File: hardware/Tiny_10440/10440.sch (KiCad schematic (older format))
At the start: 48 parts, among them J2 Battery, J3 GPIO, J4 USB_B_Micro, J5 LEDs, J7 GPIO/Power, Q1 BSS806N, Q2 BSS806N, Q3 BSS806N, Q4 BSS806N, SW1 Mode, SW2 Power, U1 STM32L072KZUx, U2 AP2210N-3.3TRG1, U3 MCP73831T-2ACI_OT, U4 ESD7002WTT1G

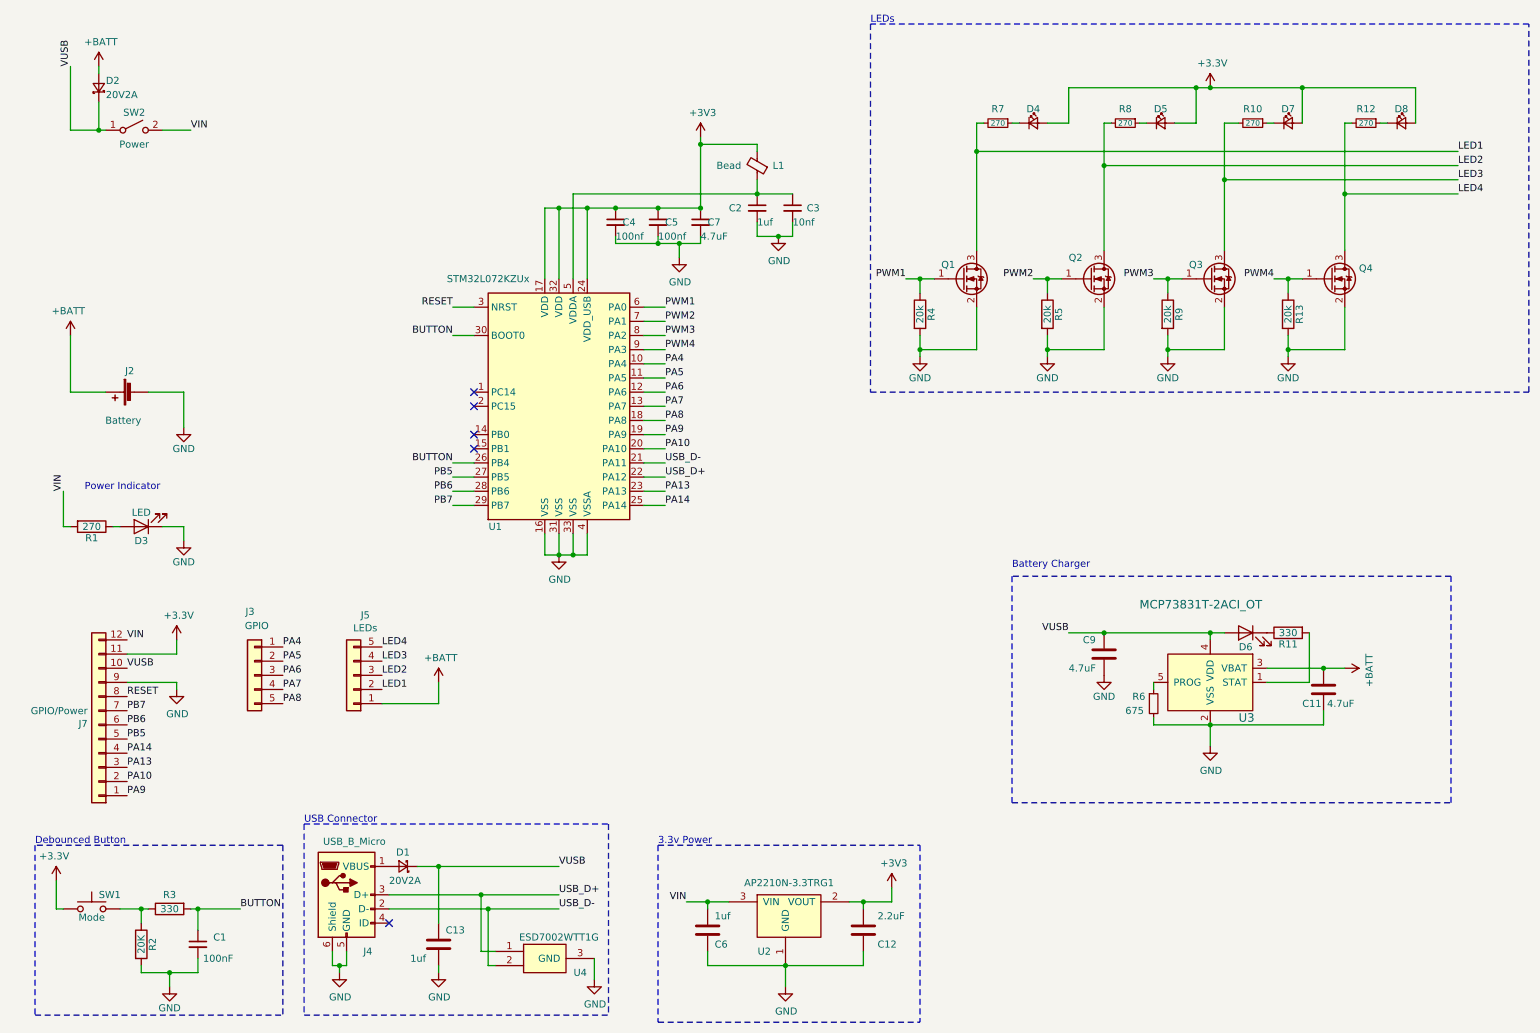
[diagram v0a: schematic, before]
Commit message: Use STM32F412CGUx (Regular & Tiny)
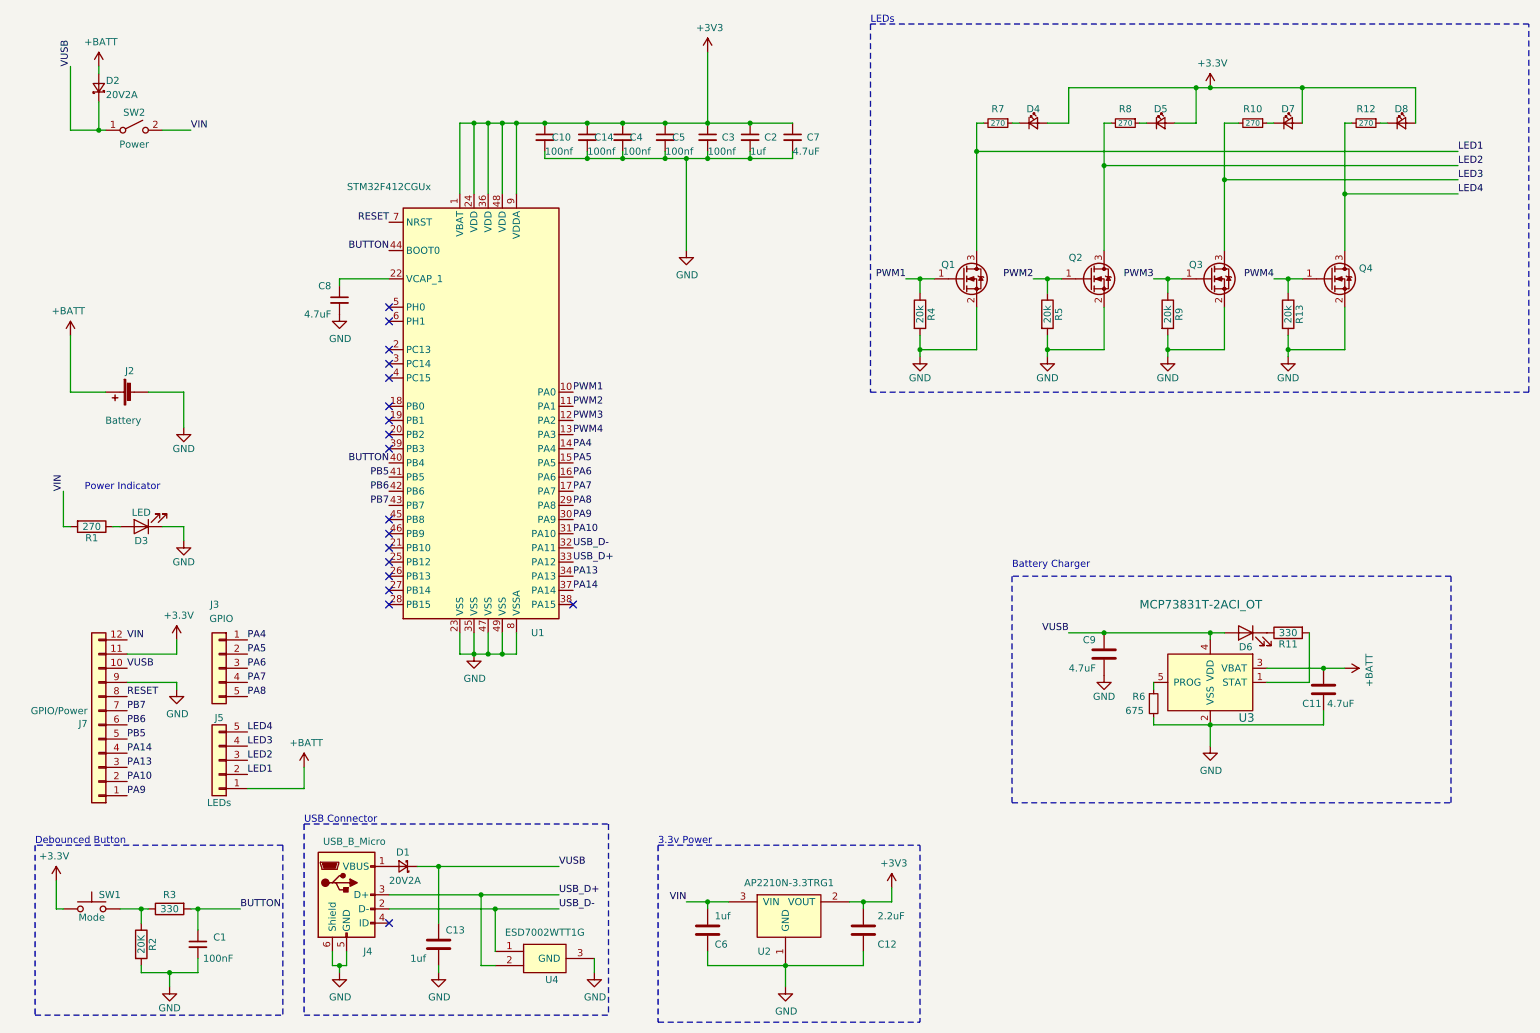
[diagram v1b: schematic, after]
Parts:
- removed L1: Bead, Inductor_SMD:L_0603_1608Metric, symbol Device:Ferrite_Bead_Small
- removed U1: STM32L072KZUx, Package_DFN_QFN:QFN-32-1EP_5x5mm_P0.5mm_EP3.45x3.45mm, symbol MCU_ST_STM32L0:STM32L072KZUx
- added C10, C14: 100nf, Capacitor_SMD:C_0603_1608Metric, symbol Device:C_Small
- added C8: 4.7uF, Capacitor_SMD:C_0603_1608Metric, symbol Device:C_Small
- added U1: STM32F412CGUx, Package_DFN_QFN:QFN-48-1EP_7x7mm_P0.5mm_EP5.6x5.6mm, symbol MCU_ST_STM32F4:STM32F412CGUx
- C3: value 10nf -> 100nf; MFN CC0603KRX7R9BB103 -> 06035C104K4T2A; MPN Yageo -> (none)
- U4: MPN ESD7002WTT1G -> (none); Package SC-70, SOT-323 -> (none)
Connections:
- net +3V3: now also C2.1, C3.1, C10.1, C14.1, U1.1 (VBAT), U1.24 (VDD), U1.36 (VDD), U1.48 (VDD), U1.9 (VDDA)
- net BUTTON: now also U1.40 (PB4), U1.44 (BOOT0)
- net GND: now also C10.2, C14.2, C8.2, U1.23 (VSS), U1.35 (VSS), U1.47 (VSS), U1.49 (VSS), U1.8 (VSSA)
- net PA10: now also U1.31 (PA10)
- net PA13: now also U1.34 (PA13)
- net PA14: now also U1.37 (PA14)
- net PA4: now also U1.14 (PA4)
- net PA5: now also U1.15 (PA5)
- net PA6: now also U1.16 (PA6)
- net PA7: now also U1.17 (PA7)
- net PA8: now also U1.29 (PA8)
- net PA9: now also U1.30 (PA9)
- net PB5: now also U1.41 (PB5)
- net PB6: now also U1.42 (PB6)
- net PB7: now also U1.43 (PB7)
- net PWM1: now also U1.10 (PA0)
- net PWM2: now also U1.11 (PA1)
- net PWM3: now also U1.12 (PA2)
- net PWM4: now also U1.13 (PA3)
- net RESET: now also U1.7 (NRST)
- net USB_D+: now also U4.2, U1.33 (PA12); no longer U4.1
- net USB_D-: now also U4.1, U1.32 (PA11); no longer U4.2
- new net: C8.1, U1.22 (VCAP_1)
- no-connect marks 5 -> 18
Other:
- moved on the sheet: C2, C3, C4, C5, C7, J3, J5
